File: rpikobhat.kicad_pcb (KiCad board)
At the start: 4 copper layers, 65 x 56 mm, 18 parts, among them J3 40HAT, J6 CONN_02X02, J9 CONN_01X02, Q1 DMG2305UX, Q2 DMMT5401, U2 CAT24C32

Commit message: Mostly done.  Need to check gerbers.
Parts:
- added C1: 0.1u, Capacitor_SMD:C_1206_3216Metric_Pad1.33x1.80mm_HandSolder, F.Cu at (101.0, 102.1)
- added C2: 10uf, Capacitor_THT:CP_Radial_D8.0mm_P5.00mm, F.Cu at (126.1, 111.1)
- added D1: MBR0560LT1G, Diode_SMD:D_SOD-123, F.Cu at (122.0, 80.4)
- added D2: MBR0560LT1G, Diode_SMD:D_SOD-123, F.Cu at (124.3, 83.7)
- added D3: MBR0560LT1G, Diode_SMD:D_SOD-123, F.Cu at (123.8, 91.6)
- added D4: 1N4004, Diode_SMD:D_SMB_Handsoldering, F.Cu at (140.6, 75.1)
- added D5: 1N4004, Diode_SMD:D_SMB_Handsoldering, F.Cu at (92.8, 111.6)
- added J1: Conn_Coaxial_Power, Connector_BarrelJack:BarrelJack_CUI_PJ-036AH-SMT_Horizontal, F.Cu at (88.9, 99.7)
- added J2: Screw_Terminal_01x02, TerminalBlock_Philmore:TerminalBlock_Philmore_TB132_1x02_P5.00mm_Horizontal, F.Cu at (83.6, 87.5)
- added J4: Screw_Terminal_01x02, TerminalBlock_Philmore:TerminalBlock_Philmore_TB132_1x02_P5.00mm_Horizontal, F.Cu at (102.6, 110.7)
- added J5: Screw_Terminal_01x02, TerminalBlock_Philmore:TerminalBlock_Philmore_TB132_1x02_P5.00mm_Horizontal, F.Cu at (114.6, 110.7)
- added Q3: IRFS4321, Package_TO_SOT_SMD:TO-263-2, F.Cu at (134.4, 98.0)
- added R1: 20.0k, Resistor_SMD:R_1206_3216Metric_Pad1.30x1.75mm_HandSolder, F.Cu at (131.1, 83.8)
- added R10: 20.0k, Resistor_SMD:R_1206_3216Metric_Pad1.30x1.75mm_HandSolder, F.Cu at (136.9, 84.6)
- added R12: R_US, Resistor_SMD:R_1206_3216Metric_Pad1.30x1.75mm_HandSolder, F.Cu at (124.0, 75.7)
- added R13: 20.0k, Resistor_SMD:R_1206_3216Metric_Pad1.30x1.75mm_HandSolder, F.Cu at (123.8, 88.1)
- added R2: 20.0k, Resistor_SMD:R_1206_3216Metric_Pad1.30x1.75mm_HandSolder, F.Cu at (116.3, 78.4)
- added R3: 20.0k, Resistor_SMD:R_1206_3216Metric_Pad1.30x1.75mm_HandSolder, F.Cu at (116.3, 81.8)
- added R4: R_US, Resistor_THT:R_Axial_DIN0414_L11.9mm_D4.5mm_P25.40mm_Horizontal, F.Cu at (99.7, 95.8)
- added R5: R_US, Resistor_THT:R_Axial_DIN0414_L11.9mm_D4.5mm_P25.40mm_Horizontal, F.Cu at (92.3, 87.5)
- added U1: LM393DR, Package_DIP:DIP-8_W7.62mm, F.Cu at (135.0, 80.0)
- J3: value 40HAT -> PI40HAT
- moved J9 0.72 mm to (113.5, 74.8)
- moved R24 0.69 mm to (88.5, 76.7)
- moved Q2 0.68 mm to (87.4, 73.0)
- moved R23 0.68 mm to (86.2, 76.7)
- moved Q1 0.34 mm to (87.4, 69.3)
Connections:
- J3 pad 10: (no net) -> unconnected-(J3-Pad10)
- J3 pad 11: (no net) -> unconnected-(J3-Pad11)
- J3 pad 12: (no net) -> unconnected-(J3-Pad12)
- J3 pad 13: (no net) -> unconnected-(J3-Pad13)
- J3 pad 15: (no net) -> unconnected-(J3-Pad15)
- J3 pad 16: (no net) -> unconnected-(J3-Pad16)
- J3 pad 17: (no net) -> unconnected-(J3-Pad17)
- J3 pad 18: (no net) -> unconnected-(J3-Pad18)
- J3 pad 19: (no net) -> unconnected-(J3-Pad19)
- J3 pad 21: (no net) -> unconnected-(J3-Pad21)
- J3 pad 22: (no net) -> unconnected-(J3-Pad22)
- J3 pad 23: (no net) -> unconnected-(J3-Pad23)
- J3 pad 24: (no net) -> unconnected-(J3-Pad24)
- J3 pad 26: (no net) -> unconnected-(J3-Pad26)
- J3 pad 29: (no net) -> unconnected-(J3-Pad29)
- J3 pad 3: (no net) -> unconnected-(J3-Pad3)
- J3 pad 31: (no net) -> unconnected-(J3-Pad31)
- J3 pad 32: (no net) -> unconnected-(J3-Pad32)
- J3 pad 33: (no net) -> unconnected-(J3-Pad33)
- J3 pad 35: (no net) -> unconnected-(J3-Pad35)
- J3 pad 36: (no net) -> unconnected-(J3-Pad36)
- J3 pad 37: (no net) -> /GPO26
- J3 pad 38: (no net) -> unconnected-(J3-Pad38)
- J3 pad 40: (no net) -> /GPI21
- J3 pad 5: (no net) -> unconnected-(J3-Pad5)
- J3 pad 7: (no net) -> unconnected-(J3-Pad7)
- J3 pad 8: (no net) -> unconnected-(J3-Pad8)
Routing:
- net /LOOP_STATE: track 0.00 -> 65.4 mm
- net /P3V3_HAT: track 2.88 -> 57.5 mm, vias 0 -> 2
- net /P5V_HAT: track 3.77 -> 57.9 mm, vias 0 -> 1
- net Net-(C1-Pad1): track 0.00 -> 49.7 mm
- net Net-(J2-Pad1): track 0.00 -> 46.1 mm
- net Net-(R2-Pad1): track 0.00 -> 28.5 mm, vias 0 -> 2
- net /GPI21: track 0.00 -> 22.8 mm
- net /OFFSET_REF_V: track 0.00 -> 22.1 mm, vias 0 -> 1
- net Net-(D3-Pad1): track 0.00 -> 16.9 mm
- net Net-(D4-Pad2): track 0.00 -> 12.6 mm
- net /GPO26: track 0.00 -> 8.97 mm
- net Net-(R12-Pad1): track 0.00 -> 6.98 mm
- net Net-(J4-Pad2): track 0.00 -> 6.96 mm
- net /P5V: track 8.71 -> 13.3 mm
- net Net-(Q1-Pad1): track 6.02 -> 6.95 mm
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- added copper zone on B.Cu, net GND
- removed copper zone on B.Cu, net /P3V3_HAT
- removed copper zone on F.Cu, net /P5V
- removed copper zone on B.Cu, net /P5V_HAT
- removed copper zone on F.Cu, net /P5V_HAT
- removed copper zone on In2.Cu, net GND
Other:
- copper layers 4 -> 2
- net class Default removed

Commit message: PCB version 1.0 complete.
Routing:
- net GND: track 0.00 -> 54.4 mm, vias 0 -> 34
- net /GPI21: track 22.8 -> 23.7 mm
- net Net-(J9-Pad2): track 9.28 -> 9.97 mm

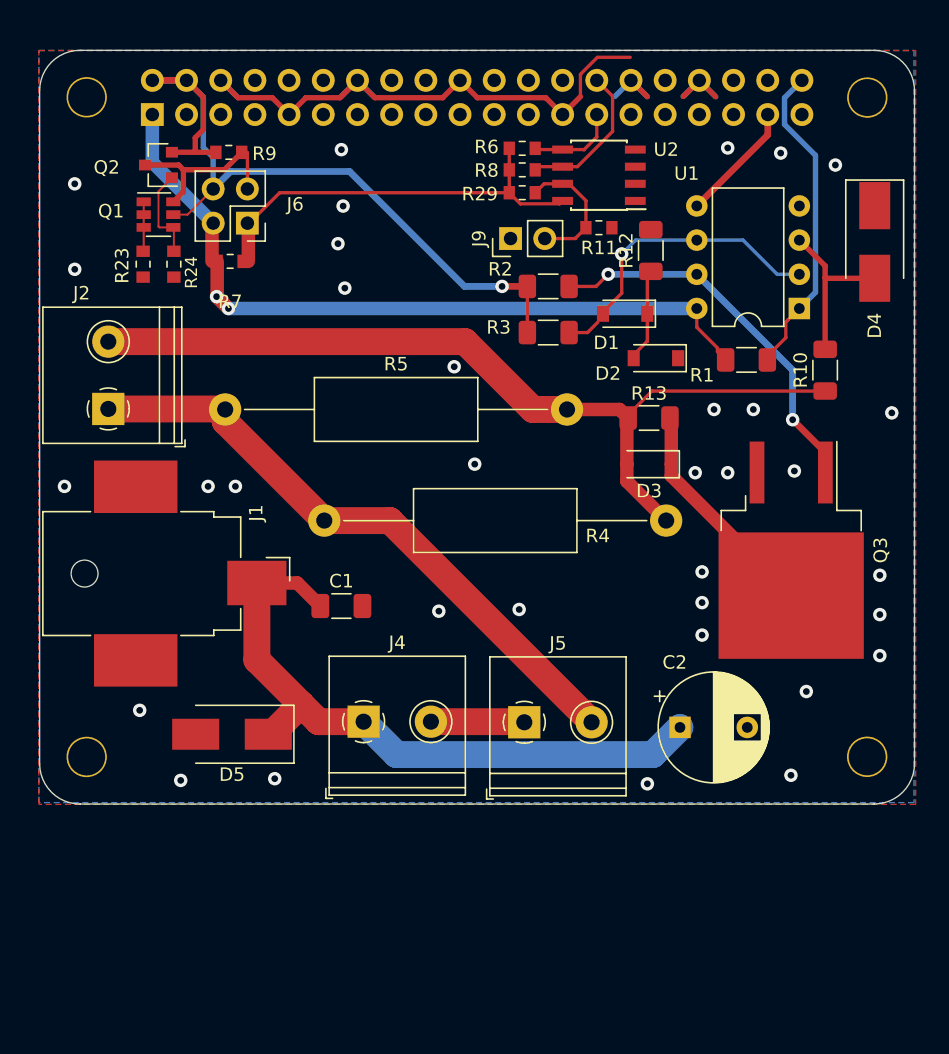
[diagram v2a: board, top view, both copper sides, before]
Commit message: Added fan, I2C port, and snubber.  General clean-up.
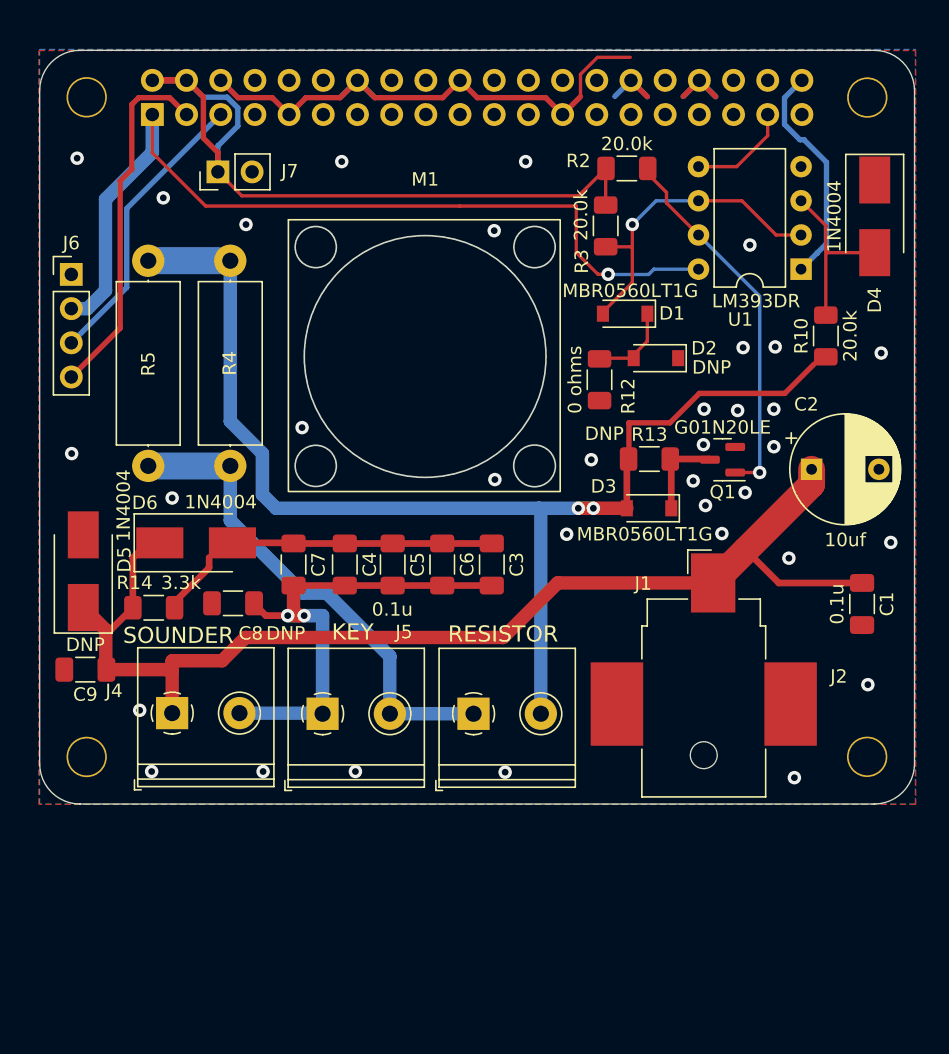
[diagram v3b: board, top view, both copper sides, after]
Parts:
- removed J9: CONN_01X02, Connector_PinHeader_2.54mm:PinHeader_1x02_P2.54mm_Vertical
- removed Q2: DMMT5401, Package_TO_SOT_SMD:SOT-23-6
- removed Q3: IRFS4321, Package_TO_SOT_SMD:TO-263-2
- removed R1: 20.0k, Resistor_SMD:R_1206_3216Metric_Pad1.30x1.75mm_HandSolder
- removed R11, R7, R9: DNP, Resistor_SMD:R_0603_1608Metric_Pad0.84x1.00mm_HandSolder
- removed R23, R29: 10K, Resistor_SMD:R_0603_1608Metric_Pad0.84x1.00mm_HandSolder
- removed R24: 47K, Resistor_SMD:R_0603_1608Metric_Pad0.84x1.00mm_HandSolder
- removed R6, R8: 3.9K, Resistor_SMD:R_0603_1608Metric_Pad0.84x1.00mm_HandSolder
- removed U2: CAT24C32, Package_SOIC:SOIC-8_3.9x4.9mm_P1.27mm
- added C3: 0.1u, Capacitor_SMD:C_1206_3216Metric_Pad1.33x1.80mm_HandSolder, F.Cu at (112.1, 99.0)
- added C4: 0.1u, Capacitor_SMD:C_1206_3216Metric_Pad1.33x1.80mm_HandSolder, F.Cu at (101.2, 99.0)
- added C5: 0.1u, Capacitor_SMD:C_1206_3216Metric_Pad1.33x1.80mm_HandSolder, F.Cu at (104.8, 99.0)
- added C6: 0.1u, Capacitor_SMD:C_1206_3216Metric_Pad1.33x1.80mm_HandSolder, F.Cu at (108.5, 99.0)
- added C7: 0.1u, Capacitor_SMD:C_1206_3216Metric_Pad1.33x1.80mm_HandSolder, F.Cu at (97.4, 99.0)
- added C8: DNP, Capacitor_SMD:C_1206_3216Metric_Pad1.33x1.80mm_HandSolder, F.Cu at (92.9, 101.9)
- added C9: DNP, Capacitor_SMD:C_1206_3216Metric_Pad1.33x1.80mm_HandSolder, F.Cu at (81.9, 106.8)
- added D6: 1N4004, Diode_SMD:D_SMB_Handsoldering, F.Cu at (90.2, 97.4)
- added J7: Conn_01x02, Connector_PinHeader_2.54mm:PinHeader_1x02_P2.54mm_Vertical, F.Cu at (91.8, 69.8)
- added M1: Fan, project_footprints:FAN_20mm, F.Cu at (107.2, 83.6)
- added R14: 3.3k, Resistor_SMD:R_1206_3216Metric_Pad1.30x1.75mm_HandSolder, F.Cu at (87.0, 102.2)
- D2: value MBR0560LT1G -> DNP
- J6: value CONN_02X02 -> Conn_01x04; footprint Connector_PinHeader_2.54mm:PinHeader_2x02_P2.54mm_Vertical -> Connector_PinHeader_2.54mm:PinHeader_1x04_P2.54mm_Vertical
- Q1: value DMG2305UX -> G01N20LE
- R12: value R_US -> 0 ohms
- R13: value 20.0k -> DNP
- R4, R5: footprint Resistor_THT:R_Axial_DIN0414_L11.9mm_D4.5mm_P25.40mm_Horizontal -> Resistor_THT:R_Axial_DIN0414_L11.9mm_D4.5mm_P15.24mm_Horizontal
- moved Q1 47.3 mm to (129.3, 91.2)
- moved J1 39.5 mm to (127.9, 106.2), turned to 0 degrees
- moved C1 38.7 mm to (139.6, 102.0), turned to -90 degrees
- moved J2 35.3 mm to (110.8, 110.1), turned to 0 degrees
- moved C2 21.5 mm to (135.9, 91.9)
- moved D5 16.4 mm to (81.8, 99.5), turned to 90 degrees
- moved J5 15.0 mm to (99.6, 110.1)
- moved J4 14.2 mm to (88.4, 110.1)
- moved J6 13.6 mm to (80.9, 77.5), turned to 0 degrees
- moved R2 10.5 mm to (122.2, 69.6)
- moved R12 10.3 mm to (120.1, 85.3), turned to -90 degrees
- moved R3 9.00 mm to (120.6, 73.9), turned to -90 degrees
- moved R4 8.08 mm to (92.7, 91.7), turned to 90 degrees
- moved R5 7.09 mm to (86.6, 91.7), turned to 90 degrees
- moved D3 3.28 mm to (123.8, 94.8)
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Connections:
- J3 pad 3: unconnected-(J3-Pad3) -> /SDA
- J3 pad 5: unconnected-(J3-Pad5) -> /SCL
- J6 pad 1: /P3V3 -> GND
- J6 pad 3: /P5V -> /SCL
- J6 pad 4: /P5V_HAT -> /SDA
- Q1 pad 2: /P5V_HAT -> GND
- Q1 pad 3: /P5V -> Net-(D3-Pad1)
- R2 pad 1: Net-(R2-Pad1) -> Net-(Q1-Pad1)
- U1 pad 7: Net-(R2-Pad1) -> Net-(Q1-Pad1)
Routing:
- net Net-(C1-Pad1): track 49.7 -> 85.8 mm
- net /P3V3: track 30.9 -> 0.00 mm
- net Net-(C3-Pad2): track 6.96 -> 37.3 mm, vias 0 -> 2
- net Net-(R2-Pad1): track 28.5 -> 0.00 mm, vias 2 -> 0
- net /SDA: track 0.00 -> 26.9 mm
- net /LOOP_STATE: track 65.4 -> 90.4 mm, vias 0 -> 2
- net Net-(C3-Pad1): track 0.00 -> 24.1 mm
- net /SCL: track 0.00 -> 21.6 mm
- net Net-(Q1-Pad1): track 6.95 -> 27.5 mm, vias 0 -> 1
- net /P5V: track 13.3 -> 0.00 mm
- net /ID_SC_EEPROM: track 11.4 -> 0.00 mm
- net Net-(D3-Pad1): track 16.9 -> 6.66 mm
- net Net-(J9-Pad2): track 9.97 -> 0.00 mm
- net /P3V3_HAT: track 57.5 -> 67.0 mm, vias 2 -> 1
- net Net-(J2-Pad1): track 46.1 -> 36.7 mm
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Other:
- board text added: "KEY"
- board text added: "RESISTOR"
- board text added: "SOUNDER"
- board text removed: "If you want to use an SMT 40-pin header, please move the top edge up by 0.5mm and locate the header in the same location as the current TH part."
- board text removed: "This is a HAT compatible PCB starting design based on the official Raspberry Pi specs at: https://github.com/raspberrypi/hats/blob/master/designguide.md Currently the camera slot and display cutout are not here. See the schematic for the details on the EEPROM and power setup. This board does have the correct components for powering the Pi via the HAT. If you need the Pi to provide 5V or 3.3V, ple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"
